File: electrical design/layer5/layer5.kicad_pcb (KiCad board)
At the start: 2 copper layers, 120 x 157.9 mm, 49 parts, among them J1 Conn_01x03_Male

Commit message: submit all pcbs for production
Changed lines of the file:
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@@
   (title_block
     (title "layer 5 pcb drawing")
-    (date "2023-02-12")
-    (rev "1.0")
+    (date "2023-02-20")
+    (rev "1.1")
     (company "8076 Robotics")
   )
@@
       (layerselection 0x00010fc_ffffffff)
       (disableapertmacros false)
-      (usegerberextensions false)
+      (usegerberextensions true)
       (usegerberattributes true)
-      (usegerberadvancedattributes true)
-      (creategerberjobfile true)
+      (usegerberadvancedattributes false)
+      (creategerberjobfile false)
       (svguseinch false)
       (svgprecision 6)
@@
       (plotinvisibletext false)
       (sketchpadsonfab false)
-      (subtractmaskfromsilk false)
+      (subtractmaskfromsilk true)
       (outputformat 1)
       (mirror false)
-      (drillshape 1)
+      (drillshape 0)
       (scaleselection 1)
-      (outputdirectory "")
+      (outputdirectory "fab/")
     )
   )
@@
     (pad "3" smd roundrect (at 1 -2) (size 0.6 1.55) (layers "F.Cu" "F.Paste" "F.Mask") (roundrect_rratio 0.25)
       (net 4 "/NEOPIXELOUT") (pinfunction "Pin_3") (pintype "passive"))
-    (pad "MP" smd roundrect (at -2.3 1.875) (size 1.2 1.8) (layers "F.Cu" "F.Paste" "F.Mask") (roundrect_rratio 0.208333))
-    (pad "MP" smd roundrect (at 2.3 1.875) (size 1.2 1.8) (layers "F.Cu" "F.Paste" "F.Mask") (roundrect_rratio 0.208333))
+    (pad "MP" smd roundrect (at -2.3 1.875) (size 1.2 1.8) (layers "F.Cu" "F.Paste" "F.Mask") (roundrect_rratio 0.2083333333))
+    (pad "MP" smd roundrect (at 2.3 1.875) (size 1.2 1.8) (layers "F.Cu" "F.Paste" "F.Mask") (roundrect_rratio 0.2083333333))
     (model "${KICAD6_3DMODEL_DIR}/Connector_JST.3dshapes/JST_SH_SM03B-SRSS-TB_1x03-1MP_P1.00mm_Horizontal.wrl"
       (offset (xyz 0 0 0))
@@
   (segment (start 122.127039 70.923199) (end 122.725548 71.268748) (width 0.25) (layer "F.Cu") (net 26))
   (segment (start 122.725548 71.268748) (end 130.756381 69.116893) (width 0.25) (layer "F.Cu") (net 26))
+  (zone (net 0) (net_name "") (layers F&B.Cu) (hatch edge 0.508)
+    (connect_pads (clearance 0))
+    (min_thickness 0.254)
+    (keepout (tracks not_allowed) (vias not_allowed) (pads not_allowed) (copperpour not_allowed) (footprints not_allowed))
+    (fill (thermal_gap 0.508) (thermal_bridge_width 0.508))
+    (polygon
+      (pts
+        (xy 120.004937 110)
+        (xy 119.985195 109.371785)
+        (xy 119.926045 108.746049)
+        (xy 119.827722 108.125262)
+        (xy 119.690614 107.511873)
+        (xy 119.515261 106.908304)
+        (xy 119.302355 106.316937)
+        (xy 119.052738 105.740105)
+        (xy 118.767393 105.180085)
+        (xy 118.447448 104.639087)
+        (xy 118.094164 104.119246)
+        (xy 117.708936 103.622613)
+        (xy 117.293285 103.151149)
+        (xy 116.848851 102.706715)
+        (xy 116.377387 102.291064)
+        (xy 115.880754 101.905836)
+        (xy 115.360913 101.552552)
+        (xy 114.819915 101.232607)
+        (xy 114.259895 100.947262)
+        (xy 113.683063 100.697645)
+        (xy 113.091696 100.484739)
+        (xy 112.488127 100.309386)
+        (xy 111.874738 100.172278)
+        (xy 111.253951 100.073955)
+        (xy 110.628215 100.014805)
+        (xy 110 99.995063)
+        (xy 109.371785 100.014805)
+        (xy 108.746049 100.073955)
+        (xy 108.125262 100.172278)
+        (xy 107.511873 100.309386)
+        (xy 106.908304 100.484739)
+        (xy 106.316937 100.697645)
+        (xy 105.740105 100.947262)
+        (xy 105.180085 101.232607)
+        (xy 104.639087 101.552552)
+        (xy 104.119246 101.905836)
+        (xy 103.622613 102.291064)
+        (xy 103.151149 102.706715)
+        (xy 102.706715 103.151149)
+        (xy 102.291064 103.622613)
+        (xy 101.905836 104.119246)
+        (xy 101.552552 104.639087)
+        (xy 101.232607 105.180085)
+        (xy 100.947262 105.740105)
+        (xy 100.697645 106.316937)
+        (xy 100.484739 106.908304)
+        (xy 100.309386 107.511873)
+        (xy 100.172278 108.125262)
+        (xy 100.073955 108.746049)
+        (xy 100.014805 109.371785)
+        (xy 99.995063 110)
+        (xy 100.014805 110.628215)
+        (xy 100.073955 111.253951)
+        (xy 100.172278 111.874738)
+        (xy 100.309386 112.488127)
+        (xy 100.484739 113.091696)
+        (xy 100.697645 113.683063)
+        (xy 100.947262 114.259895)
+        (xy 101.232607 114.819915)
+        (xy 101.552552 115.360913)
+        (xy 101.905836 115.880754)
+        (xy 102.291064 116.377387)
+        (xy 102.706715 116.848851)
+        (xy 103.151149 117.293285)
+        (xy 103.622613 117.708936)
+        (xy 104.119246 118.094164)
+        (xy 104.639087 118.447448)
+        (xy 105.180085 118.767393)
+        (xy 105.740105 119.052738)
+        (xy 106.316937 119.302355)
+        (xy 106.908304 119.515261)
+        (xy 107.511873 119.690614)
+        (xy 108.125262 119.827722)
+        (xy 108.746049 119.926045)
+        (xy 109.371785 119.985195)
+        (xy 110 120.004937)
+        (xy 110.628215 119.985195)
+        (xy 111.253951 119.926045)
+        (xy 111.874738 119.827722)
+        (xy 112.488127 119.690614)
+        (xy 113.091696 119.515261)
+        (xy 113.683063 119.302355)
+        (xy 114.259895 119.052738)
+        (xy 114.819915 118.767393)
+        (xy 115.360913 118.447448)
+        (xy 115.880754 118.094164)
+        (xy 116.377387 117.708936)
+        (xy 116.848851 117.293285)
+        (xy 117.293285 116.848851)
+        (xy 117.708936 116.377387)
+        (xy 118.094164 115.880754)
+        (xy 118.447448 115.360913)
+        (xy 118.767393 114.819915)
+        (xy 119.052738 114.259895)
+        (xy 119.302355 113.683063)
+        (xy 119.515261 113.091696)
+        (xy 119.690614 112.488127)
+        (xy 119.827722 111.874738)
+        (xy 119.926045 111.253951)
+        (xy 119.985195 110.628215)
+      )
+    )
+  )
   (zone (net 1) (net_name "+5V") (layer "F.Cu") (hatch edge 0.508)
     (connect_pads (clearance 0.508))
@@
     (members
       03a650b9-a3aa-4102-83f1-abfceac910a4
-      06cfc67f-4805-42e3-a3f4-b3dd2c46cd96
       0cc2af96-8ee5-4b27-9f41-44ed3e43571f
       0f4697bd-ec15-421c-be8a-a223ee6e52b7
@@
       164e9e34-a928-49dc-9ff3-38dd8c253e26
       19209780-ce0a-4dcb-8cc7-903600ef4973
-      1ad05ba3-d186-4618-8a7c-a22f3eeaa3da
-      1de613b1-0b55-4677-a095-3f9d1fa3442e
       223f1ec1-f255-4b45-b6b0-8feb1245083e
       27a032b9-9b72-4110-8ff5-a698532f2291
@@
       3334cfa4-2abb-4d01-af2c-06a8927901ec
       4257c773-b5a8-4589-8ffe-2a16b0e1c4d9
-      453d3e9a-1a74-4caa-b35c-67b7ea5d5e84
       5416afd4-5ff2-4fbf-b79c-7e593a155bd4
       56826c7d-daff-4e06-8aa2-af8c9cbc47f7
@@
       6c4dbdcb-df91-4842-a394-b9b99d4e613b
       79db8e42-2713-4447-b603-28fbdb383b96
-      79e6b9fd-04ab-473a-8d8b-e3cd709e7de2
       87d96173-e169-4b67-ba80-3ccb15defe43
       8e1b9099-f1ef-49bc-8fa5-e18cf88e8640
       92fd29a5-39ed-4fa4-9433-ee1fa4fa4d2e
-      95b516a0-600e-4ccc-bfdd-af89d79917d2
-      960b204b-82d7-4420-8aa3-dffb6618d0c2
       96d4462d-1c7c-4e9a-a71a-59ba3cd96240
       a8c69bf1-ac95-4534-ad8a-504d04da967f
@@
       dae9cf26-bdec-4e29-925c-ccd8ea5edea8
       dfb58ec5-5755-4727-a8b2-fc28f34879cb
-      e9679a76-e330-4154-9cc2-6031abf5b66a
       ee45bc49-303b-4747-92bf-0309c4715e53
       ee942d6c-7306-4463-b164-18da1830d4af
@@
     )
   )
+  (group "screwholes" locked (id 4e69790e-56a5-4e6f-848a-274669a1c9f7)
+    (members
+      06cfc67f-4805-42e3-a3f4-b3dd2c46cd96
+      1ad05ba3-d186-4618-8a7c-a22f3eeaa3da
+      1de613b1-0b55-4677-a095-3f9d1fa3442e
+      453d3e9a-1a74-4caa-b35c-67b7ea5d5e84
+      79e6b9fd-04ab-473a-8d8b-e3cd709e7de2
+      95b516a0-600e-4ccc-bfdd-af89d79917d2
+      960b204b-82d7-4420-8aa3-dffb6618d0c2
+      e9679a76-e330-4154-9cc2-6031abf5b66a
+    )
+  )

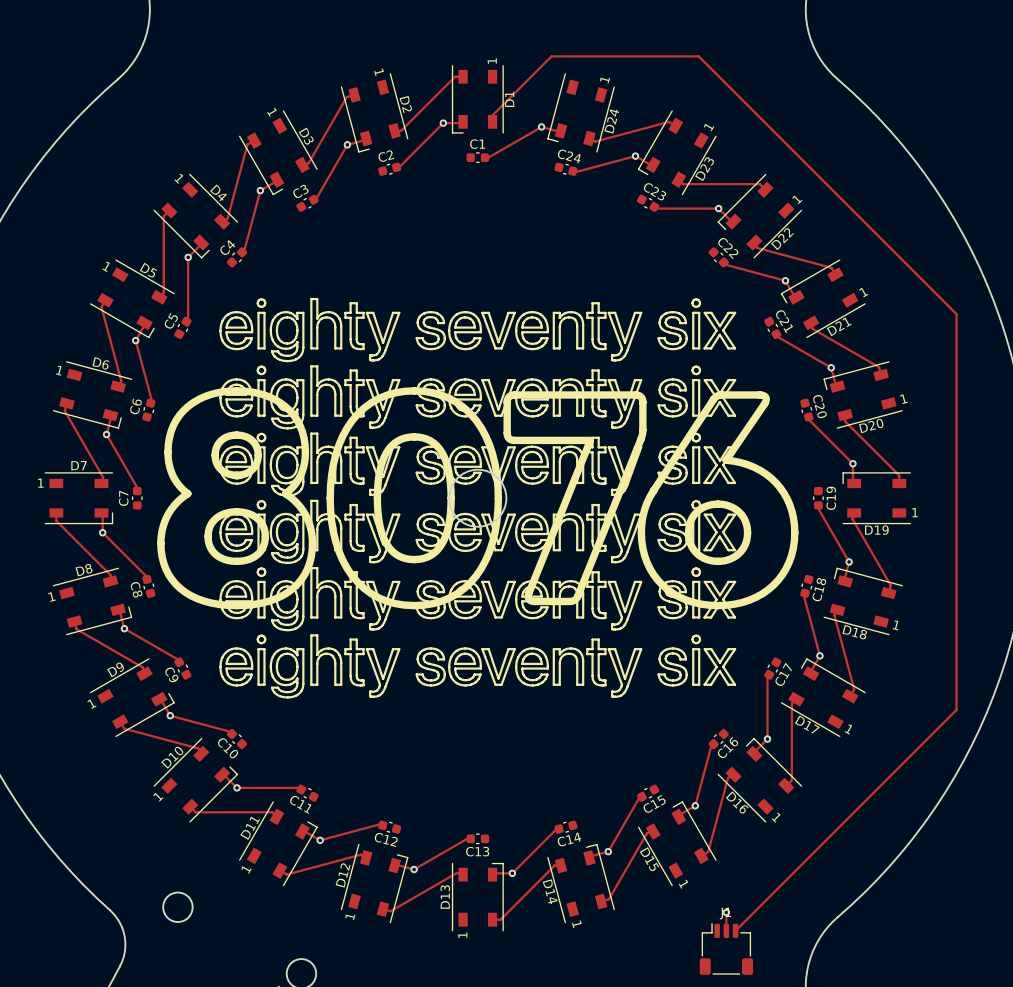
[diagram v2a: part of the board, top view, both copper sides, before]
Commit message: fillet pcb traces
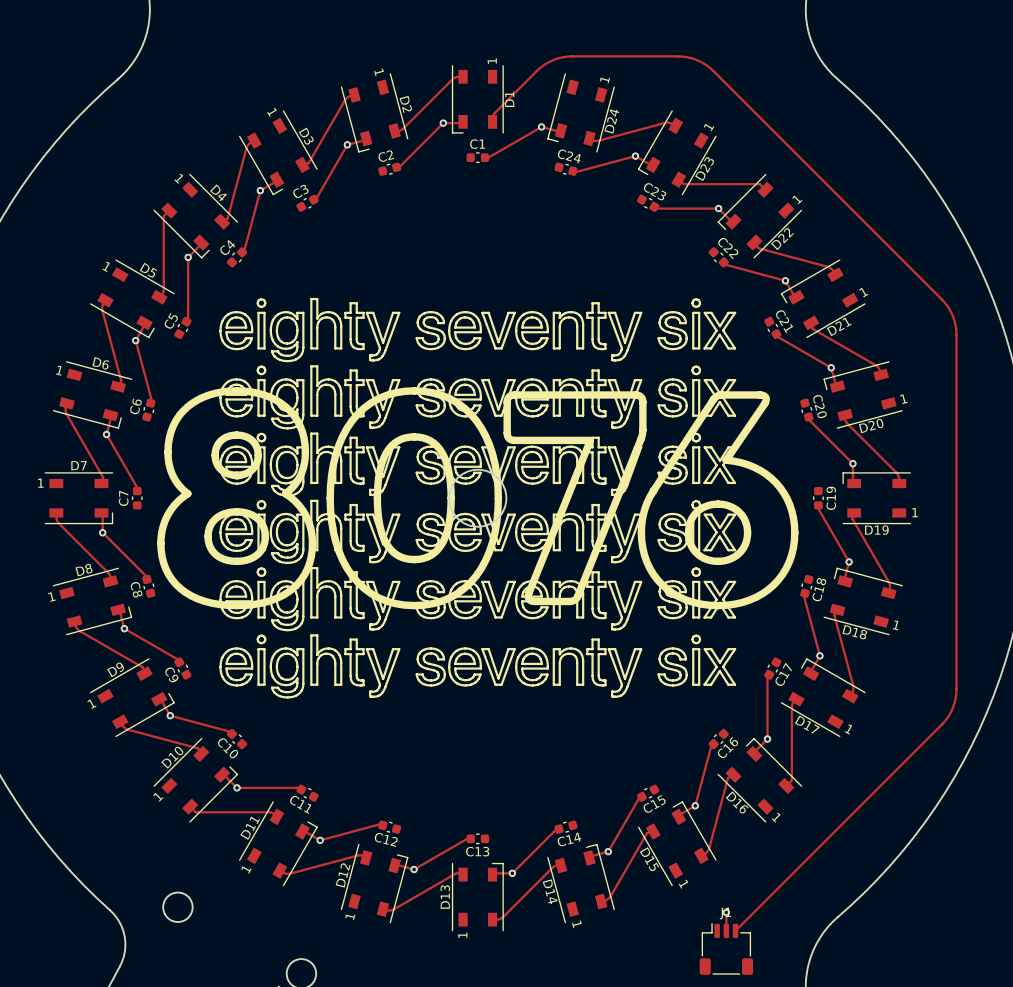
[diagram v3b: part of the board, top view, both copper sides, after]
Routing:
- net /NEOPIXELOUT: track 142.3 -> 141.2 mm
